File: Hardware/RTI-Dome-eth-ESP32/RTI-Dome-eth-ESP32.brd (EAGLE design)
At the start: 111.1 x 76.3 mm, 96 parts, among them IC1 LM2675MX-5.0_NOPB, IC2 24LC64T-I/SN, IC8 REG1117-3.3V, J1 691313510003, J10 691313510002, J11 691313510002, J12 691313510002, J2 XT60PW-M, J3 691313510003, J4 691313510003, J6 691313510003, J7 691313510003, J8 691313510002, J9 691313510002, T1 MMBT3904LT1, T2 MMBT3904LT1, T3 MMBT3904LT1, U1 W5500, U2 ESP32-DevKitC-32UE, X9 J1011F01PNL

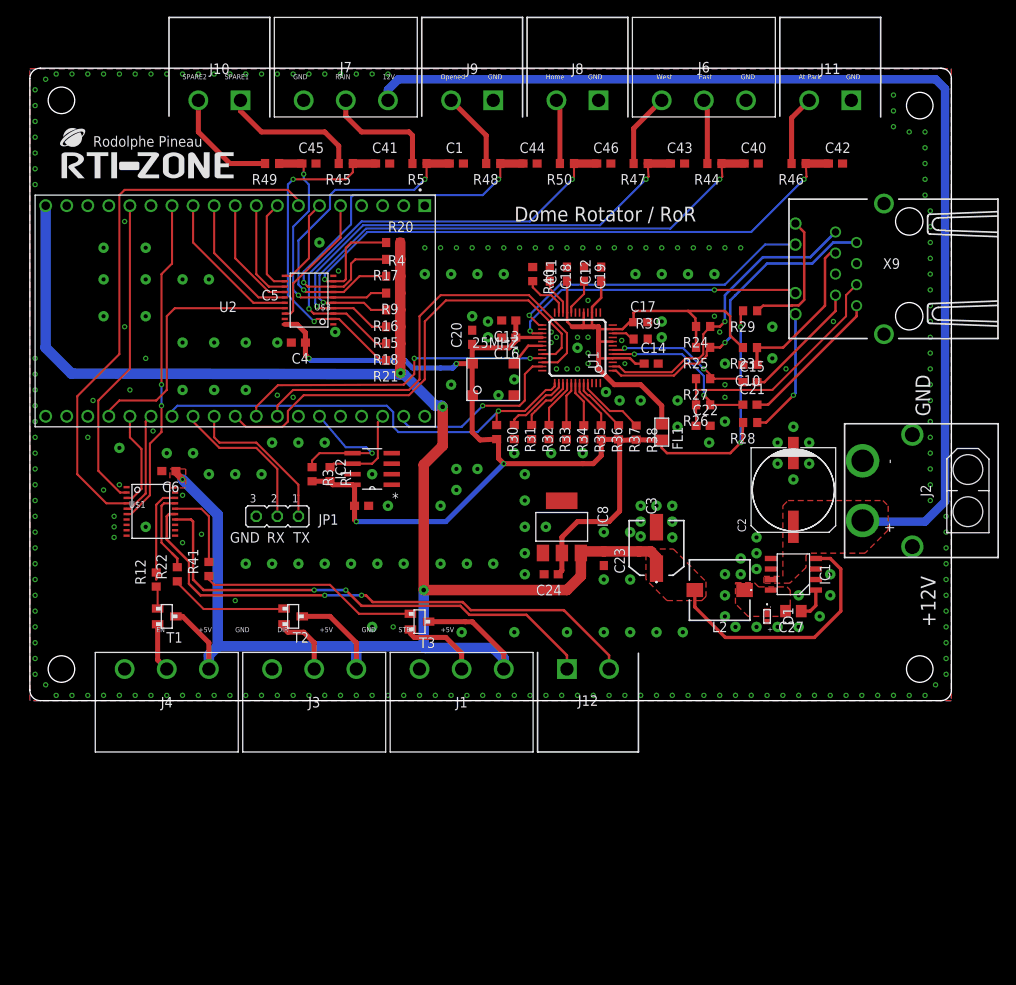
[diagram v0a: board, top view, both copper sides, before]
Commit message: New ESP32 firmware is working.
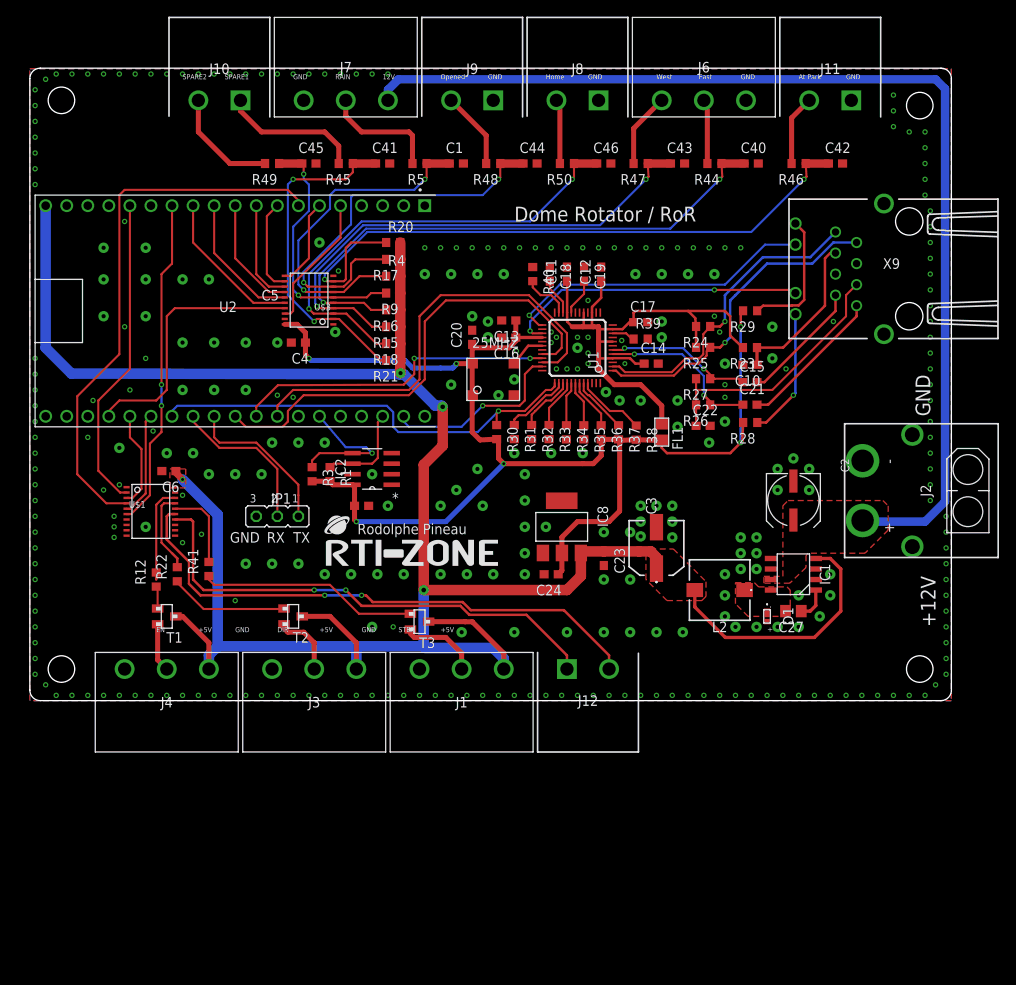
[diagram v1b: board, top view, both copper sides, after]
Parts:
- C2: device samacsys:UD-10X10_NICHICON -> rcl:UD-6,3X7,7_NICHICON
- moved U$4 56.6 mm to (35.7, 16.3)
- moved C2 1.27 mm to (92.1, 24.1), turned to 270 degrees
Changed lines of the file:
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@@
 <attribute name="VALUE" x="47.625" y="67.31" size="1.27" layer="27" rot="R180"/>
 </element>
-<element name="U$4" library="rti" library_urn="urn:adsk.eagle:library:37256580" package="LOGO_BIG" package3d_urn="urn:adsk.eagle:package:37318421/1" value="RTI-LOGO_BIG" x="3.81" y="62.992" smashed="yes"/>
+<element name="U$4" library="rti" library_urn="urn:adsk.eagle:library:37256580" package="LOGO_BIG" package3d_urn="urn:adsk.eagle:package:37318421/1" value="RTI-LOGO_BIG" x="35.687" y="16.256" smashed="yes"/>
 <element name="R15" library="rcl" library_urn="urn:adsk.eagle:library:334" package="R0603" package3d_urn="urn:adsk.eagle:package:23555/3" value="4.7K" x="43.815" y="45.085" smashed="yes" rot="R180">
 <attribute name="MPN" value="RT0805FRE074K7L" x="43.815" y="45.085" size="1.778" layer="27" rot="R180" display="off"/>
@@
 <attribute name="VALUE" x="24.13" y="15.24" size="1.27" layer="27" rot="R90"/>
 </element>
-<element name="U2" library="ESP32-DEVKITC-32D" library_urn="urn:adsk.eagle:library:44270575" package="MODULE_ESP32-DEVKITC-32U" package3d_urn="urn:adsk.eagle:package:44294361/4" value="ESP32-DevKitC-32UE" x="27.305" y="46.99" smashed="yes" rot="R270">
+<element name="U2" library="ESP32-DEVKITC-32D" library_urn="urn:adsk.eagle:library:44270575" package="MODULE_ESP32-DEVKITC-32U" package3d_urn="urn:adsk.eagle:package:44294361/7" value="ESP32-DevKitC-32UE" x="27.305" y="46.99" smashed="yes" rot="R270">
 <attribute name="NAME" x="22.8246" y="46.8608" size="1.270490625" layer="25"/>
 <attribute name="VALUE" x="-1.6252" y="61.0046" size="1.27133125" layer="27" rot="R270"/>
 </element>
-<element name="JP1" library="rti" library_urn="urn:adsk.eagle:library:37256580" package="JP2" package3d_urn="urn:adsk.eagle:package:37318384/1" value="" x="29.845" y="22.225" smashed="yes" rot="R180">
-<attribute name="NAME" x="37.211" y="22.479" size="1.27" layer="25" ratio="10" rot="R180"/>
+<element name="JP1" library="rti" library_urn="urn:adsk.eagle:library:37256580" package="JP2" package3d_urn="urn:adsk.eagle:package:37318384/2" value="" x="29.845" y="22.225" smashed="yes" rot="R180">
+<attribute name="NAME" x="31.496" y="25.019" size="1.27" layer="25" ratio="10" rot="R180"/>
 <attribute name="VALUE" x="33.401" y="26.543" size="1.27" layer="27" ratio="10" rot="R180"/>
 </element>
@@
 <attribute name="VALUE" x="86.36" y="10.16" size="1.27" layer="27" rot="R270" align="center"/>
 </element>
-<element name="C2" library="samacsys" library_urn="urn:adsk.eagle:library:37256869" package="UD-10X10_NICHICON" package3d_urn="urn:adsk.eagle:package:38013982/9" value="100uF" x="92.075" y="25.4" smashed="yes" rot="R90">
-<attribute name="MPN" value="C249838" x="92.075" y="25.4" size="1.778" layer="27" rot="R90" display="off"/>
-<attribute name="NAME" x="86.36" y="20.32" size="1.016" layer="25" rot="R90"/>
-<attribute name="VALUE" x="98.425" y="20.32" size="1.016" layer="27" rot="R90"/>
+<element name="C2" library="rcl" library_urn="urn:adsk.eagle:library:334" package="UD-6,3X7,7_NICHICON" package3d_urn="urn:adsk.eagle:package:23472/1" value="100uF" x="92.075" y="24.13" smashed="yes" rot="R270">
+<attribute name="JLCPCB" value="VZH101M1VTR-0607" x="92.075" y="24.13" size="1.778" layer="27" rot="R270" display="off"/>
+<attribute name="MPN" value="VZH101M1VTR-0607
+" x="92.075" y="24.13" size="1.778" layer="27" rot="R270" display="off"/>
+<attribute name="NAME" x="97.79" y="29.21" size="1.016" layer="25" rot="R270"/>
+<attribute name="POPULARITY" value="1" x="92.075" y="24.13" size="1.778" layer="27" rot="R270" display="off"/>
+<attribute name="SPICEPREFIX" value="C" x="92.075" y="24.13" size="1.778" layer="27" rot="R270" display="off"/>
+<attribute name="VALUE" x="85.725" y="29.21" size="1.016" layer="27" rot="R270"/>
 </element>
 <element name="C3" library="samacsys" library_urn="urn:adsk.eagle:library:37256869" package="EEEHP1H4R7P" package3d_urn="urn:adsk.eagle:package:45493987/6" value="68uF" x="75.565" y="18.415" smashed="yes" rot="R90">
@@
 <via x="78.105" y="33.02" extent="1-16" drill="0.5" diameter="1.27"/>
 <via x="62.23" y="20.955" extent="1-16" drill="0.5" diameter="1.27"/>
-<via x="51.435" y="27.94" extent="1-16" drill="0.5" diameter="1.27"/>
+<via x="54.61" y="23.495" extent="1-16" drill="0.5" diameter="1.27"/>
 <via x="69.215" y="20.32" extent="1-16" drill="0.5" diameter="1.27"/>
 <via x="73.66" y="36.195" extent="1-16" drill="0.5" diameter="1.27"/>
@@
 <via x="22.225" y="37.465" extent="1-16" drill="0.5" diameter="1.27"/>
 <via x="18.415" y="37.465" extent="1-16" drill="0.5" diameter="1.27"/>
-<via x="85.725" y="17.145" extent="1-16" drill="0.5" diameter="1.27"/>
+<via x="85.725" y="17.78" extent="1-16" drill="0.5" diameter="1.27"/>
 <via x="73.66" y="19.812" extent="1-16" drill="0.5" diameter="1.27"/>
 <via x="87.63" y="15.875" extent="1-16" drill="0.5" diameter="1.27"/>
-<via x="90.17" y="31.115" extent="1-16" drill="0.5" diameter="1.27"/>
-<via x="93.98" y="31.115" extent="1-16" drill="0.5" diameter="1.27"/>
-<via x="92.075" y="26.67" extent="1-16" drill="0.5" diameter="1.27"/>
+<via x="90.17" y="27.94" extent="1-16" drill="0.5" diameter="1.27"/>
+<via x="85.725" y="19.685" extent="1-16" drill="0.5" diameter="1.27"/>
+<via x="93.98" y="25.4" extent="1-16" drill="0.5" diameter="1.27"/>
 <via x="96.52" y="15.24" extent="1-16" drill="0.5" diameter="1.27"/>
 <via x="87.63" y="17.78" extent="1-16" drill="0.5" diameter="1.27"/>
@@
 <via x="92.71" y="12.7" extent="1-16" drill="0.5" diameter="1.27"/>
 <via x="96.52" y="12.7" extent="1-16" drill="0.5" diameter="1.27"/>
-<via x="85.725" y="15.24" extent="1-16" drill="0.5" diameter="1.27"/>
+<via x="85.725" y="15.875" extent="1-16" drill="0.5" diameter="1.27"/>
 <via x="76.2" y="43.815" extent="1-16" drill="0.5" diameter="1.27"/>
 <via x="55.245" y="45.72" extent="1-16" drill="0.5" diameter="1.27"/>
@@
 <via x="95.25" y="10.16" extent="1-16" drill="0.5" diameter="1.27"/>
 <via x="75.565" y="23.495" extent="1-16" drill="0.5" diameter="1.27"/>
-<via x="92.075" y="33.02" extent="1-16" drill="0.5" diameter="1.27"/>
-<via x="93.98" y="28.575" extent="1-16" drill="0.5" diameter="1.27"/>
-<via x="90.17" y="28.575" extent="1-16" drill="0.5" diameter="1.27"/>
+<via x="92.075" y="29.21" extent="1-16" drill="0.5" diameter="1.27"/>
+<via x="93.98" y="27.94" extent="1-16" drill="0.5" diameter="1.27"/>
+<via x="90.17" y="25.4" extent="1-16" drill="0.5" diameter="1.27"/>
 <via x="62.865" y="44.45" extent="1-16" drill="0.35"/>
 <via x="69.469" y="37.211" extent="1-16" drill="0.5" diameter="1.27"/>
@@
 <via x="29.21" y="16.51" extent="1-16" drill="0.5" diameter="1.27"/>
 <via x="32.385" y="16.51" extent="1-16" drill="0.5" diameter="1.27"/>
-<via x="35.56" y="16.51" extent="1-16" drill="0.5" diameter="1.27"/>
-<via x="38.735" y="16.51" extent="1-16" drill="0.5" diameter="1.27"/>
-<via x="41.91" y="16.51" extent="1-16" drill="0.5" diameter="1.27"/>
-<via x="45.085" y="16.51" extent="1-16" drill="0.5" diameter="1.27"/>
-<via x="49.53" y="16.51" extent="1-16" drill="0.5" diameter="1.27"/>
-<via x="52.705" y="16.51" extent="1-16" drill="0.5" diameter="1.27"/>
-<via x="55.88" y="16.51" extent="1-16" drill="0.5" diameter="1.27"/>
+<via x="35.56" y="15.24" extent="1-16" drill="0.5" diameter="1.27"/>
+<via x="38.735" y="15.24" extent="1-16" drill="0.5" diameter="1.27"/>
+<via x="41.91" y="15.24" extent="1-16" drill="0.5" diameter="1.27"/>
+<via x="45.085" y="15.24" extent="1-16" drill="0.5" diameter="1.27"/>
+<via x="49.53" y="15.24" extent="1-16" drill="0.5" diameter="1.27"/>
+<via x="52.705" y="15.24" extent="1-16" drill="0.5" diameter="1.27"/>
+<via x="55.88" y="15.24" extent="1-16" drill="0.5" diameter="1.27"/>
 <via x="43.18" y="23.495" extent="1-16" drill="0.5" diameter="1.27"/>
 <via x="51.435" y="25.4" extent="1-16" drill="0.5" diameter="1.27"/>

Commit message: Changing 5V circuit
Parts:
- added C25: 10uF, rcl:C0805
- added C26: 22uF, rcl:C0805
- added C29: 1uF, rcl:C0805
- added C7: 10uF, rcl:C1206
- added C8: 0.1uF, rcl:C1206
- added C9: 3.3nF, rcl:C0805
- added L1: IHLP1212BZER2R2M11, samacsys:INDPM3630X200N
- added PS1: TPS62133RGTR, samacsys:QFN50P300X300X100-17N
- added R7: 100K, rcl:R0603
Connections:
- new net PG: PS1.4, R7.2
- new net SS/TR: C9.1, PS1.9
- new net SW: L1.1, PS1.1, PS1.2, PS1.3
- net +12V: now also C7.1, C8.1, PS1.10, PS1.11, PS1.12, PS1.13
- net GND: now also C25.1, C26.1, C29.1, C7.2, C8.2, C9.2, PS1.15, PS1.16, PS1.17, PS1.5, PS1.6, PS1.7, PS1.8
- net VCC: now also C25.2, C26.2, C29.2, L1.2, PS1.14, R7.1

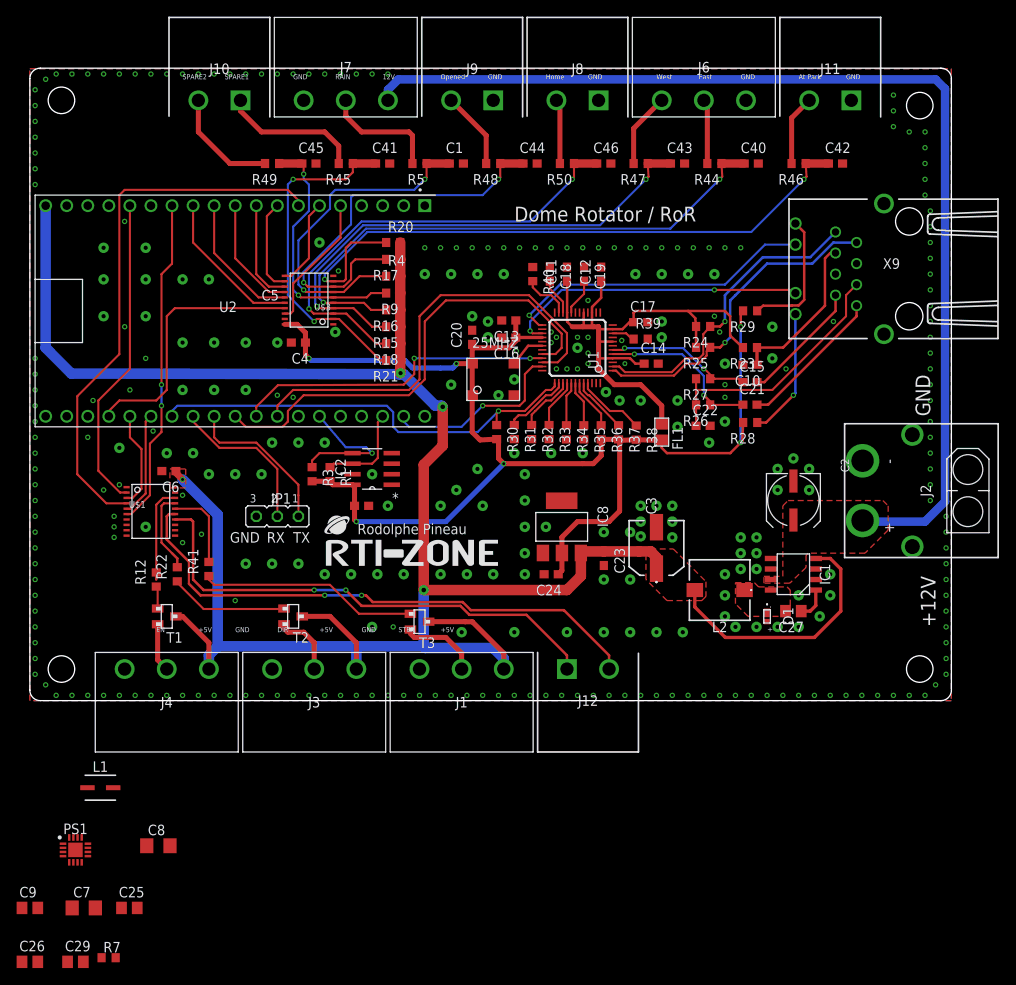
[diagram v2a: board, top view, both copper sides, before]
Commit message: New 5V circuit routed
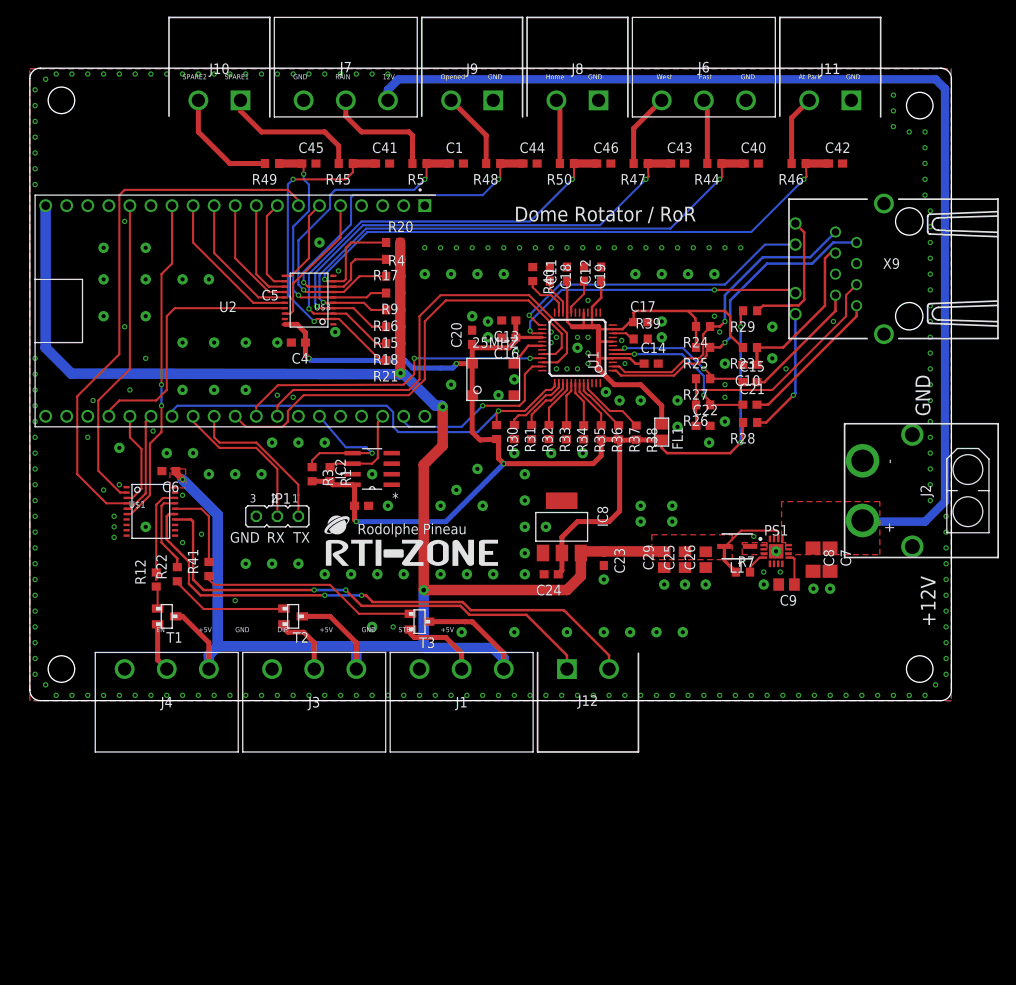
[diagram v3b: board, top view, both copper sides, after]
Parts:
- removed C2: 100uF, rcl:UD-6,3X7,7_NICHICON
- removed C27: 10nF, rcl:C0805
- removed C3: 68uF, samacsys:EEEHP1H4R7P
- removed D1: PMEG4015EPK,315, samacsys:PMEG4015EPK315
- removed IC1: LM2675MX-5.0_NOPB, samacsys:SOIC127P600X175-8N
- removed L2: 47uH, samacsys:784777470
- moved C7 99.3 mm to (96.5, 17.0), turned to 270 degrees
- moved C9 99.2 mm to (91.2, 14.0), turned to 180 degrees
- moved C26 94.8 mm to (81.5, 17.0), turned to 90 degrees
- moved PS1 91.8 mm to (90.0, 18.0)
- moved R7 89.5 mm to (86.0, 15.5)
- moved C8 86.2 mm to (94.5, 17.0), turned to 270 degrees
- moved C29 86.0 mm to (76.5, 17.0), turned to 90 degrees
- moved L1 82.1 mm to (85.3, 18.6), turned to 180 degrees
- moved C25 79.1 mm to (79.0, 17.0), turned to 90 degrees
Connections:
- removed net N$2: C27.1, IC1.1
- removed net SWV: C27.2, D1.1, IC1.8, L2.1
- net +12V: no longer C2.+, IC1.7
- net GND: no longer C2.-, C3.2, D1.2, IC1.6
- net VCC: no longer C3.1, IC1.4, L2.2
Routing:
- net VCC: track 275.7 -> 255.8 mm
- net N$2: track 3.90 -> 0.00 mm
- net SS/TR: track 0.00 -> 3.86 mm
- net PG: track 0.00 -> 2.73 mm
- added copper zone on layer 1, net SW
- removed copper zone on layer 1, net SWV
